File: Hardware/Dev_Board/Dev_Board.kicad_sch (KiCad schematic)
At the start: 0 parts

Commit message: Added EEPROM documentation
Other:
- added sheet EEPROM (eeprom.kicad_sch)
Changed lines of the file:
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@@
+		)
+	)
+	(sheet
+		(at 194.31 86.36)
+		(size 12.7 7.62)
+		(fields_autoplaced yes)
+		(stroke
+			(width 0.1524)
+			(type solid)
+		)
+		(fill
+			(color 0 0 0 0.0000)
+		)
+		(property "Sheetname" "EEPROM"
+			(at 194.31 85.6484 0)
+			(effects
+				(font
+					(size 1.27 1.27)
+				)
+				(justify left bottom)
+			)
+		)
+		(property "Sheetfile" "eeprom.kicad_sch"
+			(at 194.31 94.5646 0)
+			(effects
+				(font
+					(size 1.27 1.27)
+				)
+				(justify left top)
+			)
+		)
+		(pin "SCL" bidirectional
+			(at 194.31 88.9 180)
+			(effects
+				(font
+					(size 1.27 1.27)
+				)
+				(justify left)
+			)
+		)
+		(pin "SDA" bidirectional
+			(at 194.31 91.44 180)
+			(effects
+				(font
+					(size 1.27 1.27)
+				)
+				(justify left)
+			)
+		)
+		(instances
+			(project "Dev_Board"
+				(path "/ab11133b-b546-4233-b741-8575932eb964"
+					(page "3")
+				)
+			)
 		)
 	)

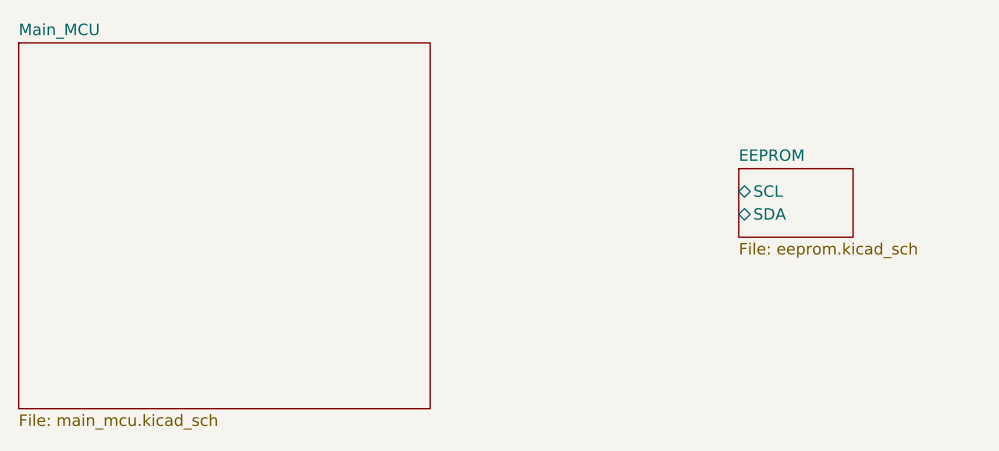
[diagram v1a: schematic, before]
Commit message: Added the temperature sensor
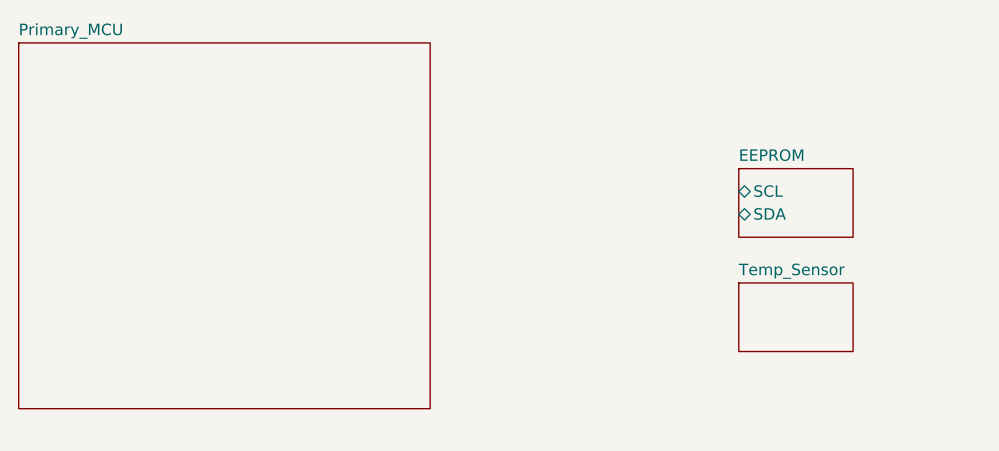
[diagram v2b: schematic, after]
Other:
- sheet Main_MCU renamed Primary_MCU
- added sheet Temp_Sensor (temp_sensor.kicad_sch)
- sheet Primary_MCU: file main_mcu.kicad_sch -> primary_mcu.kicad_sch
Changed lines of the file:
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@@
 			(color 0 0 0 0.0000)
 		)
-		(property "Sheetname" "Main_MCU"
+		(property "Sheetname" "Primary_MCU"
 			(at 114.3 71.6784 0)
 			(effects
@@
 			)
 		)
-		(property "Sheetfile" "main_mcu.kicad_sch"
+		(property "Sheetfile" "primary_mcu.kicad_sch"
 			(at 114.3 113.6146 0)
 			(effects
@@
 				)
 				(justify left top)
+				(hide yes)
 			)
 		)
@@
 				(path "/ab11133b-b546-4233-b741-8575932eb964"
 					(page "2")
+				)
+			)
+		)
+	)
+	(sheet
+		(at 194.31 99.06)
+		(size 12.7 7.62)
+		(fields_autoplaced yes)
+		(stroke
+			(width 0.1524)
+			(type solid)
+		)
+		(fill
+			(color 0 0 0 0.0000)
+		)
+		(property "Sheetname" "Temp_Sensor"
+			(at 194.31 98.3484 0)
+			(effects
+				(font
+					(size 1.27 1.27)
+				)
+				(justify left bottom)
+			)
+		)
+		(property "Sheetfile" "temp_sensor.kicad_sch"
+			(at 194.31 107.2646 0)
+			(effects
+				(font
+					(size 1.27 1.27)
+				)
+				(justify left top)
+				(hide yes)
+			)
+		)
+		(instances
+			(project "Dev_Board"
+				(path "/ab11133b-b546-4233-b741-8575932eb964"
+					(page "4")
 				)
 			)
@@
 				)
 				(justify left top)
+				(hide yes)
 			)
 		)
